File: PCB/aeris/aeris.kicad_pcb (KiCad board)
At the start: 2 copper layers, 48 x 37 mm, 18 parts, among them J1 BATT+, J2 BATT-, J5 PulseIN, J6 PulseOUT, J7 Conn_01x04_Pin, Q1 FS8205A, U1 DW01A, U2 MCP1700T-3302E, U3 ESP32-H2-SUPERMINI

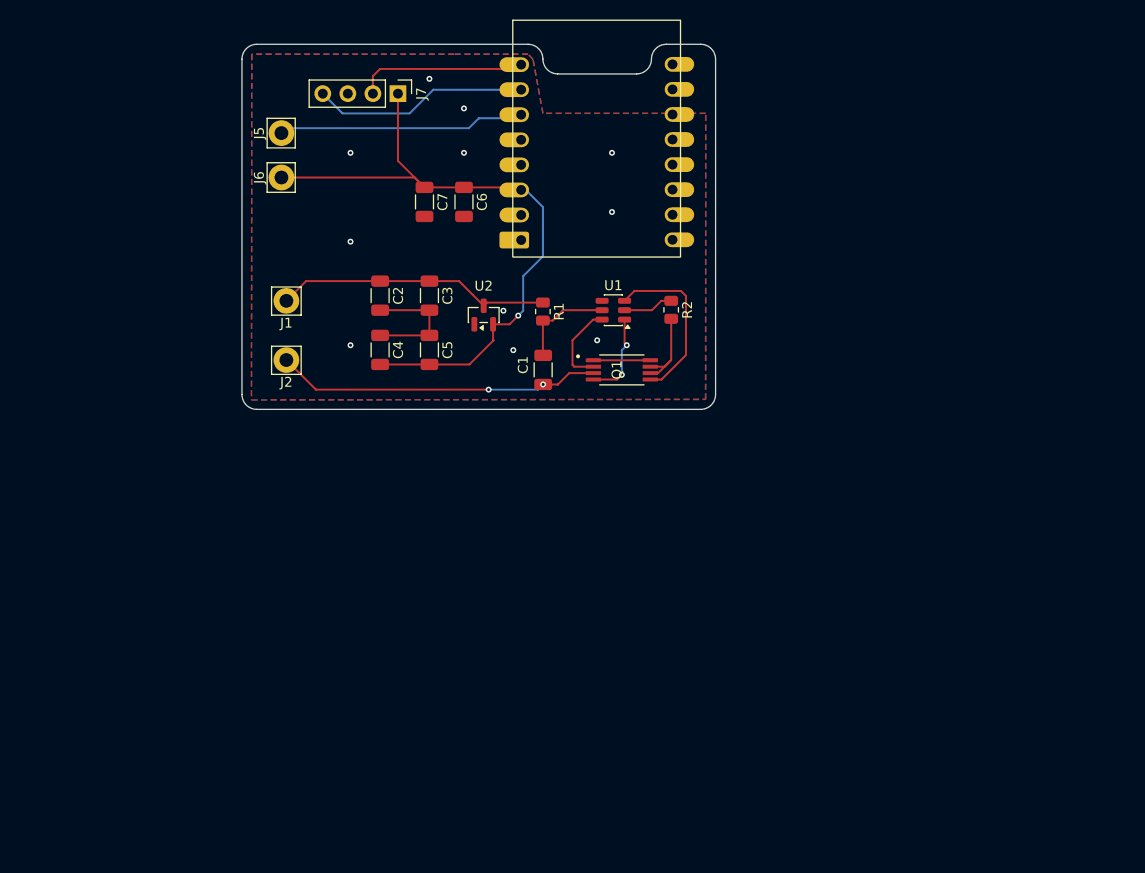
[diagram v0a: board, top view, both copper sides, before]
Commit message: PCB version 1.0 Update PIN assignment for better PCB routing
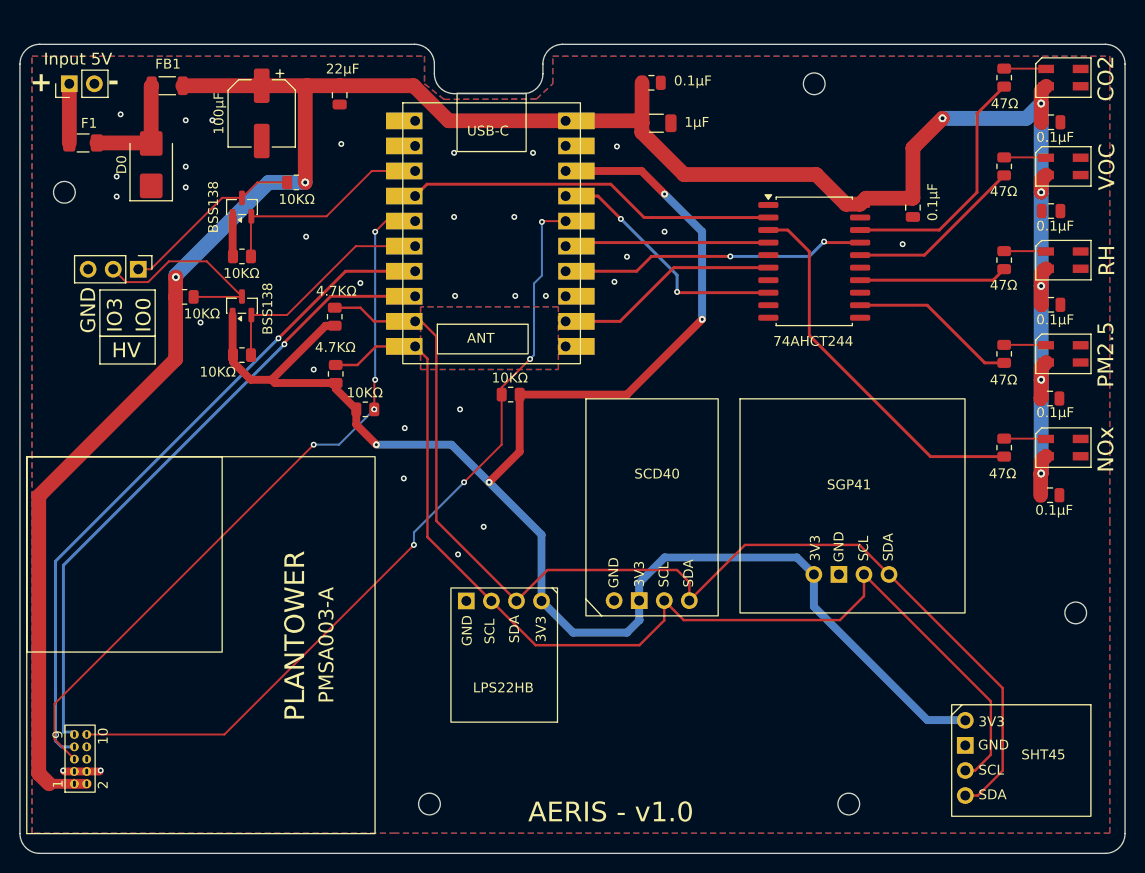
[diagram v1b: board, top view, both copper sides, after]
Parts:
- removed U3: ESP32-H2-SUPERMINI, esp32-h2-supermini:ESP32H2-Supermini
- added C10: 0.1µF, Capacitor_SMD:C_0805_2012Metric, F.Cu at (125.5, 44.5)
- added C8: 0.1µF, Capacitor_SMD:C_0805_2012Metric, F.Cu at (139.5, 35.9)
- added C9: 0.1µF, Capacitor_SMD:C_0805_2012Metric, F.Cu at (139.5, 44.9)
- added D0: D_TVS, Diode_SMD:D_SMB, F.Cu at (48.3, 40.2)
- added D1: SK6812MINI, LED_SMD:LED_SK6812MINI_PLCC4_3.5x3.5mm_P1.75mm, F.Cu at (140.8, 31.4)
- added D2: SK6812MINI, LED_SMD:LED_SK6812MINI_PLCC4_3.5x3.5mm_P1.75mm, F.Cu at (140.8, 40.4)
- added D3: SK6812MINI, LED_SMD:LED_SK6812MINI_PLCC4_3.5x3.5mm_P1.75mm, F.Cu at (140.8, 49.9)
- added D4: SK6812MINI, LED_SMD:LED_SK6812MINI_PLCC4_3.5x3.5mm_P1.75mm, F.Cu at (140.8, 59.4)
- added D5: SK6812MINI, LED_SMD:LED_SK6812MINI_PLCC4_3.5x3.5mm_P1.75mm, F.Cu at (140.8, 68.9)
- added F1: Fuse_Small, Fuse:Fuse_1206_3216Metric, F.Cu at (41.4, 38.0)
- added FB1: FerriteBead, Inductor_SMD:L_1206_3216Metric, F.Cu at (49.9, 32.2)
- added H1: MountingHole, MountingHole:MountingHole_2.2mm_M2, F.Cu at (119.0, 105.0)
- added H2: MountingHole, MountingHole:MountingHole_2.2mm_M2, F.Cu at (142.0, 85.6)
- added H3: MountingHole, MountingHole:MountingHole_2.2mm_M2, F.Cu at (39.5, 43.0)
- added H4: MountingHole, MountingHole:MountingHole_2.2mm_M2, F.Cu at (115.5, 32.0)
- added H5: MountingHole, MountingHole:MountingHole_2.2mm_M2, F.Cu at (76.5, 105.0)
- added J3: LPS22HB, esp32-h2-supermini:LPS22HB-Breakout, F.Cu at (83.8, 90.2)
- added J4: SCD40, esp32-h2-supermini:SCD40-Breakout, F.Cu at (99.3, 78.6)
- added Q2: BSS138, Package_TO_SOT_SMD:SOT-23, F.Cu at (57.5, 54.5)
- added R10: 47R, Resistor_SMD:R_0805_2012Metric, F.Cu at (134.8, 40.4)
- added R11: 47R, Resistor_SMD:R_0805_2012Metric, F.Cu at (134.8, 49.9)
- added R12: 47R, Resistor_SMD:R_0805_2012Metric, F.Cu at (134.8, 59.4)
- added R13: 47R, Resistor_SMD:R_0805_2012Metric, F.Cu at (134.8, 68.9)
- added R3: 10KΩ, Resistor_SMD:R_0805_2012Metric, F.Cu at (70.0, 65.0)
- added R4: 10KΩ, Resistor_SMD:R_0805_2012Metric, F.Cu at (84.7, 63.5)
- added R5: 10K, Resistor_SMD:R_0805_2012Metric, F.Cu at (57.5, 49.5)
- added R6: 10K, Resistor_SMD:R_0805_2012Metric, F.Cu at (57.5, 59.5)
- added R7: 10K, Resistor_SMD:R_0805_2012Metric, F.Cu at (63.0, 42.0)
- added R8: 10K, Resistor_SMD:R_0805_2012Metric, F.Cu at (51.7, 53.6)
- added R9: 47R, Resistor_SMD:R_0805_2012Metric, F.Cu at (134.8, 31.4)
- C1: value 0.1µF -> 1µF
- C2, C6: value 1µF -> 0.1µF; footprint Capacitor_SMD:C_1206_3216Metric -> Capacitor_SMD:C_0805_2012Metric
- C3: value 0.1µF -> 100µF; footprint Capacitor_SMD:C_1206_3216Metric -> Capacitor_SMD:CP_Elec_6.3x5.9
- C4: value 1µF -> 22µF; footprint Capacitor_SMD:C_1206_3216Metric -> Capacitor_SMD:C_0805_2012Metric
- C5, C7: footprint Capacitor_SMD:C_1206_3216Metric -> Capacitor_SMD:C_0805_2012Metric
- J1: value BATT+ -> PMSA003A; footprint Connector_Pin:Pin_D1.4mm_L8.5mm_W2.8mm_FlatFork -> esp32-h2-supermini:PLANTOWER_PMSA003-A
- J2: value BATT- -> SHT45; footprint Connector_Pin:Pin_D1.4mm_L8.5mm_W2.8mm_FlatFork -> esp32-h2-supermini:SHT45-Breakout
- J5: value PulseIN -> SGP41; footprint Connector_Pin:Pin_D1.4mm_L8.5mm_W2.8mm_FlatFork -> esp32-h2-supermini:SGP41-Breakout
- J6: value PulseOUT -> USB-C Input; footprint Connector_Pin:Pin_D1.4mm_L8.5mm_W2.8mm_FlatFork -> Connector_PinHeader_2.54mm:PinHeader_1x02_P2.54mm_Vertical
- J7: value Conn_01x04_Pin -> OUT; footprint Connector_PinHeader_2.54mm:PinHeader_1x04_P2.54mm_Vertical -> Connector_PinHeader_2.54mm:PinHeader_1x03_P2.54mm_Vertical
- Q1: value FS8205A -> BSS138; footprint FS8205A:SOP65P640X120-8N -> Package_TO_SOT_SMD:SOT-23
- R1: value 100R -> 4.7K
- R2: value 1K -> 4.7K
- U1: value DW01A -> ESP32-C6-SUPERMINI; footprint Package_TO_SOT_SMD:SOT-23-6 -> esp32-h2-supermini:ESP32C6-Supermini
- U2: value MCP1700T-3302E -> 74AHCT244; footprint Package_TO_SOT_SMD:SOT-23 -> Package_SO:SOIC-20W_7.5x12.8mm_P1.27mm
- moved J2 84.9 mm to (136.6, 100.6), turned to -90 degrees
- moved C7 70.0 mm to (139.4, 73.7), turned to 0 degrees
- moved J5 69.2 mm to (119.4, 74.9), turned to 0 degrees
- moved C5 63.2 mm to (139.5, 54.4), turned to 0 degrees
- moved C6 62.7 mm to (139.4, 63.9), turned to 0 degrees
- moved Q1 41.9 mm to (57.5, 44.5), turned to 90 degrees
- moved J1 36.0 mm to (53.3, 88.9), turned to 90 degrees
- moved C2 35.0 mm to (99.0, 31.9), turned to 0 degrees
- moved R2 34.6 mm to (67.0, 61.4)
- moved U2 33.9 mm to (115.5, 50.0), turned to 0 degrees
- moved J7 31.8 mm to (47.0, 50.8)
- moved C1 27.5 mm to (99.5, 36.0), turned to 0 degrees
- moved C4 26.1 mm to (67.4, 33.1), turned to 90 degrees
- moved C3 25.1 mm to (59.5, 35.0)
- moved J6 23.5 mm to (40.0, 32.0), turned to 90 degrees
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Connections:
- C1 pad 1: Net-(U1-VCC) -> +5V
- C1 pad 2: BATT- -> GND
- C2 pad 1: BATT+ -> +5V
- C2 pad 2: OUT- -> GND
- C3 pad 1: BATT+ -> +5V
- C3 pad 2: OUT- -> GND
- C4 pad 1: OUT- -> GND
- C4 pad 2: +3V3 -> +5V
- C5 pad 1: OUT- -> +5V
- C5 pad 2: +3V3 -> GND
- C6 pad 1: +3V3 -> +5V
- C6 pad 2: OUT- -> GND
- C7 pad 1: +3V3 -> +5V
- C7 pad 2: OUT- -> GND
- J1 pad 1: BATT+ -> +5V
- J2 pad 1: BATT- -> +3V3
- J5 pad 1: GPIO12 -> +3V3
- J6 pad 1: +3V3 -> Net-(J6-Pin_1)
- J7 pad 1: +3V3 -> GPIO0HV
- J7 pad 2: SDA -> GPIO3HV
- J7 pad 3: OUT- -> GND
- Q1 pad 1: Net-(Q1-Pad1) -> +3V3
- Q1 pad 2: BATT- -> GPIO0
- Q1 pad 3: BATT- -> GPIO0HV
- R1 pad 1: BATT+ -> +3V3
- R1 pad 2: Net-(U1-VCC) -> SDA
- R2 pad 1: Net-(U1-CS) -> SCL
- R2 pad 2: OUT- -> +3V3
- U1 pad 1: Net-(U1-OD) -> unconnected-(U1-IO8-Pad1)
- U1 pad 2: Net-(U1-CS) -> GPIO9
- U1 pad 3: Net-(U1-OC) -> unconnected-(U1-IO14-Pad3)
- U1 pad 4: unconnected-(U1-TD-Pad4) -> GPIO15
- U1 pad 5: Net-(U1-VCC) -> GPIO18
- U1 pad 6: BATT- -> GPIO19
- U2 pad 1: OUT- -> GND
- U2 pad 2: +3V3 -> GPIO1
- U2 pad 3: BATT+ -> NOx
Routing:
- net +5V: track 0.00 -> 247.5 mm, vias 0 -> 8
- net +3V3: track 70.2 -> 179.6 mm, vias 1 -> 4
- net SDA: track 17.3 -> 116.2 mm
- net SCL: track 21.9 -> 111.4 mm
- net GPIO19: track 0.00 -> 81.7 mm, vias 0 -> 4
- net GPIO2: track 0.00 -> 73.7 mm, vias 0 -> 4
- net TX: track 0.00 -> 69.0 mm, vias 0 -> 1
- net RX: track 0.00 -> 65.2 mm, vias 0 -> 1
- net BATT-: track 41.6 -> 0.00 mm, vias 2 -> 0
- net NOx: track 0.00 -> 38.4 mm
- net GPIO1: track 0.00 -> 37.7 mm
- net GPIO15: track 0.00 -> 31.0 mm, vias 0 -> 2
- net BATT+: track 28.7 -> 0.00 mm
- net GPIO20: track 0.00 -> 25.6 mm, vias 0 -> 2
- net CO2: track 0.00 -> 25.3 mm
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- added copper zone on B.Cu, net GND
- added copper zone on F.Cu, net GND
- removed copper zone on B.Cu, net OUT-
- removed copper zone on F.Cu, net OUT-
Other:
- board size 48 x 37 mm -> 112 x 82 mm
- board text added: "+"
- board text added: "-"
- board text added: "0.1µF"
- board text added: "1"
- board text added: "10"
- board text added: "10KΩ"
- board text added: "2"
- board text added: "3V3"
- board text added: "4.7KΩ"
- board text added: "47Ω"
- board text added: "9"
- board text added: "AERIS - v1.0"
- board text added: "CO2"
- board text added: "GND"
- board text added: "HV"
- board text added: "IO0"
- board text added: "IO3"
- board text added: "Input 5V"
- board text added: "NOx"
- board text added: "PM2.5"
- board text added: "RH"
- board text added: "SCL"
- board text added: "SDA"
- board text added: "VOC"
